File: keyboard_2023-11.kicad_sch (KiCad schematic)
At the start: 70 parts, among them J1 Conn_01x04, J11 Conn_01x07_Socket, J2 Conn_01x04_Socket, J3 Conn_01x07_Socket, J4 Conn_01x07_Pin, SW1 SW_Push, SW10 SW_Push, SW11 SW_Push, SW12 SW_Push, SW13 SW_Push, SW14 SW_Push, SW15 SW_Push, SW16 SW_Push, SW17 SW_Push, SW18 SW_Push, SW19 SW_Push, SW2 SW_Push, SW20 SW_Push, SW21 SW_Push, SW22 SW_Push, SW23 SW_Push, SW24 SW_Push, SW3 SW_Push, SW4 SW_Push, SW5 SW_Push, SW6 SW_Push, SW7 SW_Push, SW8 SW_Push, SW9 SW_Push, U1 MCP23017_SO, U2 MCP23017_SO

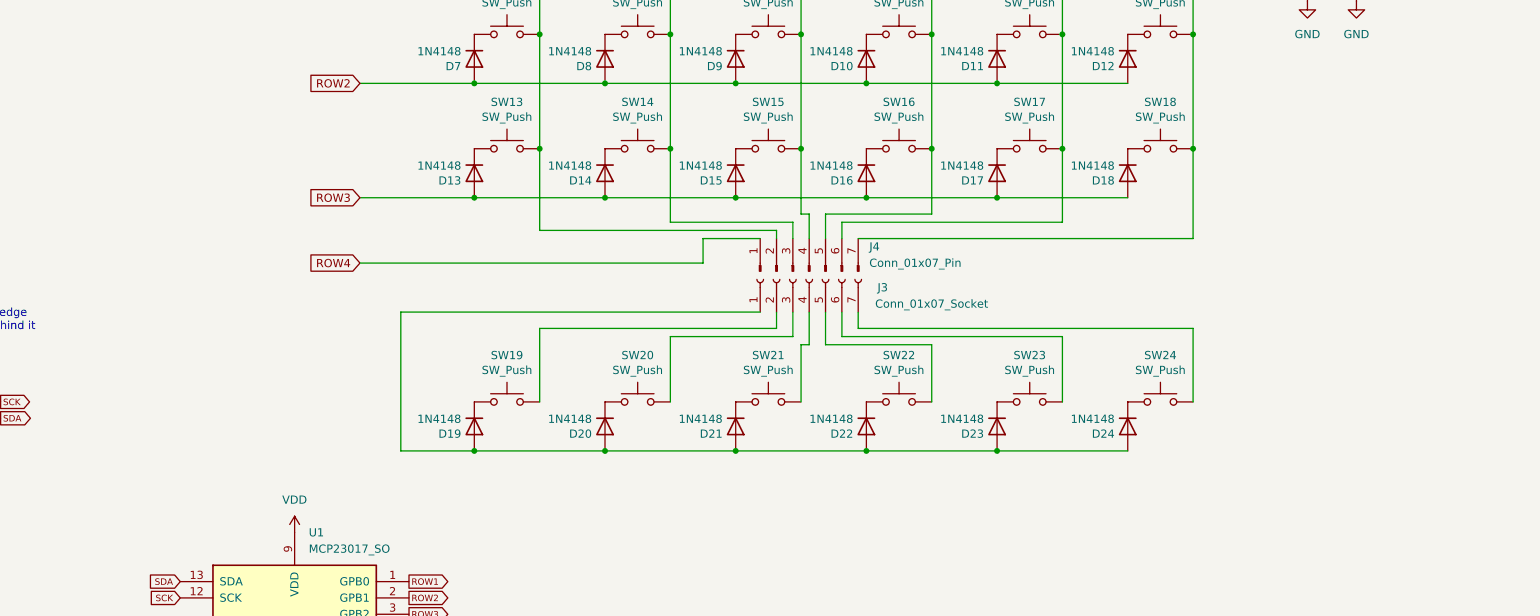
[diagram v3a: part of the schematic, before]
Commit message: better solder jumpers?
adding a solder mask cutout where the pads are default-connected, to better see which part needs to be scrached out

Signed-off-by: Johannes <you@example.com>
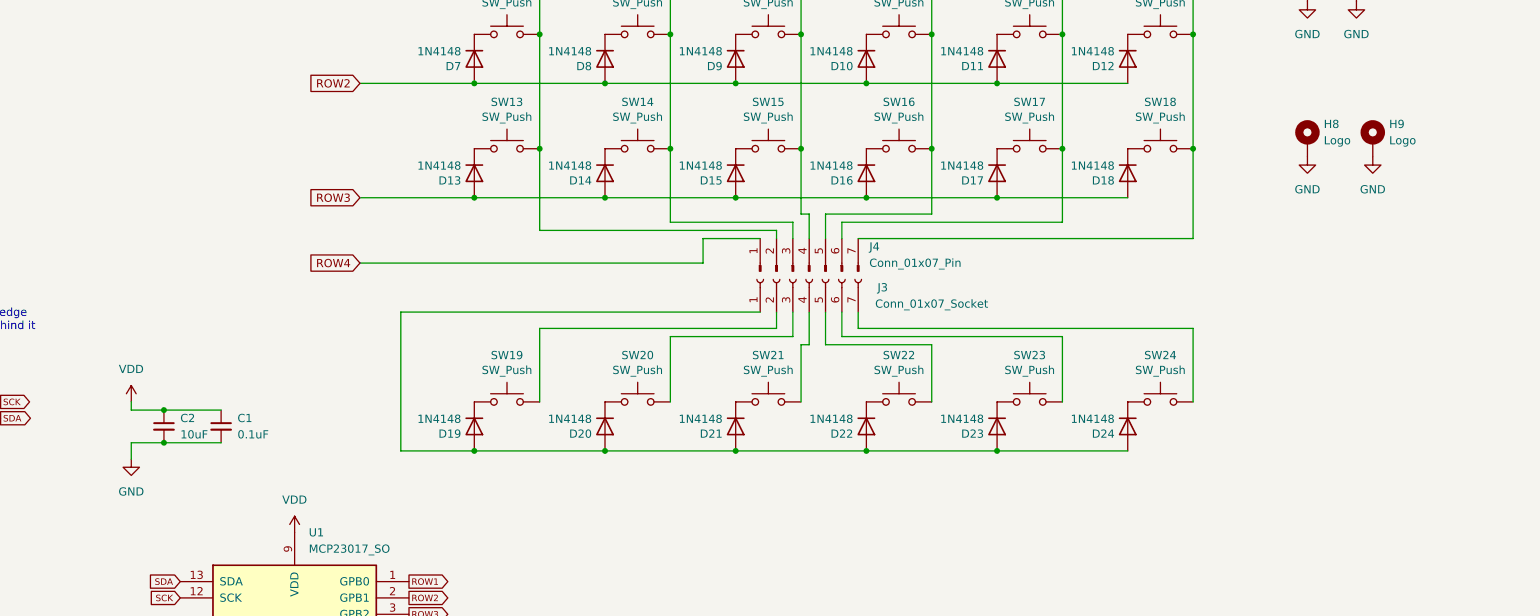
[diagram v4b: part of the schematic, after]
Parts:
- added C1: 0.1uF, reversible-kicad:C-0805_2012Metric, symbol Device:C_Small
- added C2: 10uF, reversible-kicad:C-0805_2012Metric, symbol Device:C_Small
- added H8, H9: Logo, project-local:logo, symbol Mechanical:MountingHole_Pad
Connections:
- net GND: now also C1.2, C2.2, H8.1, H9.1
- net VDD: now also C1.1, C2.1
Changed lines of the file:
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@@
 (kicad_sch (version 20230121) (generator eeschema)
   (paper "A4")
+  (junction (at 71.12 106.68) (diameter 0) (color 0 0 0 0)
+  )
   (junction (at 210.82 66.04) (diameter 0) (color 0 0 0 0)
   )
@@
   )
   (junction (at 190.5 29.21) (diameter 0) (color 0 0 0 0)
+  )
+  (junction (at 71.12 111.76) (diameter 0) (color 0 0 0 0)
   )
   (junction (at 43.18 176.53) (diameter 0) (color 0 0 0 0)
@@
     (stroke (width 0) (type default))
   )
+  (wire (pts (xy 66.04 105.41) (xy 66.04 106.68))
+    (stroke (width 0) (type default))
+  )
   (wire (pts (xy 160.02 55.88) (xy 180.34 55.88))
     (stroke (width 0) (type default))
@@
     (stroke (width 0) (type default))
   )
+  (wire (pts (xy 66.04 111.76) (xy 66.04 114.3))
+    (stroke (width 0) (type default))
+  )
+  (wire (pts (xy 66.04 106.68) (xy 71.12 106.68))
+    (stroke (width 0) (type default))
+  )
   (wire (pts (xy 119.38 113.03) (xy 139.7 113.03))
     (stroke (width 0) (type default))
@@
     (stroke (width 0) (type default))
   )
+  (wire (pts (xy 71.12 106.68) (xy 80.01 106.68))
+    (stroke (width 0) (type default))
+  )
   (wire (pts (xy 71.12 243.84) (xy 74.93 243.84))
     (stroke (width 0) (type default))
@@
     (stroke (width 0) (type default))
   )
+  (wire (pts (xy 71.12 111.76) (xy 80.01 111.76))
+    (stroke (width 0) (type default))
+  )
   (wire (pts (xy 41.91 39.37) (xy 34.29 39.37))
     (stroke (width 0) (type default))
@@
   )
   (wire (pts (xy 163.83 91.44) (xy 107.95 91.44))
+    (stroke (width 0) (type default))
+  )
+  (wire (pts (xy 71.12 111.76) (xy 66.04 111.76))
     (stroke (width 0) (type default))
   )
@@
     )
   )
+  (symbol (lib_id "power:VDD") (at 66.04 105.41 0) (unit 1)
+    (in_bom yes) (on_board yes) (dnp no) (fields_autoplaced)
+    (property "Reference" "#PWR025" (at 66.04 109.22 0)
+      (effects (font (size 1.27 1.27)) hide)
+    )
+    (property "Value" "VDD" (at 66.04 100.33 0)
+      (effects (font (size 1.27 1.27)))
+    )
+    (property "Footprint" "" (at 66.04 105.41 0)
+      (effects (font (size 1.27 1.27)) hide)
+    )
+    (property "Datasheet" "" (at 66.04 105.41 0)
+      (effects (font (size 1.27 1.27)) hide)
+    )
+    (pin "1")
+    (instances
+      (project "keyboard_2023-11"
+        (path "/182f2ae4-37a2-476f-8f08-1d2b242ef345"
+          (reference "#PWR025") (unit 1)
+        )
+      )
+    )
+  )
+  (symbol (lib_id "power:GND") (at 66.04 114.3 0) (unit 1)
+    (in_bom yes) (on_board yes) (dnp no) (fields_autoplaced)
+    (property "Reference" "#PWR026" (at 66.04 120.65 0)
+      (effects (font (size 1.27 1.27)) hide)
+    )
+    (property "Value" "GND" (at 66.04 119.38 0)
+      (effects (font (size 1.27 1.27)))
+    )
+    (property "Footprint" "" (at 66.04 114.3 0)
+      (effects (font (size 1.27 1.27)) hide)
+    )
+    (property "Datasheet" "" (at 66.04 114.3 0)
+      (effects (font (size 1.27 1.27)) hide)
+    )
+    (pin "1")
+    (instances
+      (project "keyboard_2023-11"
+        (path "/182f2ae4-37a2-476f-8f08-1d2b242ef345"
+          (reference "#PWR026") (unit 1)
+        )
+      )
+    )
+  )
   (symbol (lib_id "Device:D") (at 220.98 52.07 270) (unit 1)
     (in_bom yes) (on_board yes) (dnp no)
@@
     )
   )
+  (symbol (lib_id "Device:C_Small") (at 71.12 109.22 0) (unit 1)
+    (in_bom yes) (on_board yes) (dnp no) (fields_autoplaced)
+    (property "Reference" "C2" (at 73.66 107.9563 0)
+      (effects (font (size 1.27 1.27)) (justify left))
+    )
+    (property "Value" "10uF" (at 73.66 110.4963 0)
+      (effects (font (size 1.27 1.27)) (justify left))
+    )
+    (property "Footprint" "reversible-kicad:C-0805_2012Metric" (at 71.12 109.22 0)
+      (effects (font (size 1.27 1.27)) hide)
+    )
+    (property "Datasheet" "~" (at 71.12 109.22 0)
+      (effects (font (size 1.27 1.27)) hide)
+    )
+    (pin "1")
+    (pin "2")
+    (instances
+      (project "keyboard_2023-11"
+        (path "/182f2ae4-37a2-476f-8f08-1d2b242ef345"
+          (reference "C2") (unit 1)
+        )
+      )
+    )
+  )
+  (symbol (lib_id "Device:C_Small") (at 80.01 109.22 0) (unit 1)
+    (in_bom yes) (on_board yes) (dnp no) (fields_autoplaced)
+    (property "Reference" "C1" (at 82.55 107.9563 0)
+      (effects (font (size 1.27 1.27)) (justify left))
+    )
+    (property "Value" "0.1uF" (at 82.55 110.4963 0)
+      (effects (font (size 1.27 1.27)) (justify left))
+    )
+    (property "Footprint" "reversible-kicad:C-0805_2012Metric" (at 80.01 109.22 0)
+      (effects (font (size 1.27 1.27)) hide)
+    )
+    (property "Datasheet" "~" (at 80.01 109.22 0)
+      (effects (font (size 1.27 1.27)) hide)
+    )
+    (pin "1")
+    (pin "2")
+    (instances
+      (project "keyboard_2023-11"
+        (path "/182f2ae4-37a2-476f-8f08-1d2b242ef345"
+          (reference "C1") (unit 1)
+        )
+      )
+    )
+  )
   (symbol (lib_id "Device:D") (at 119.38 52.07 270) (unit 1)
     (in_bom yes) (on_board yes) (dnp no)
@@
     )
   )
+  (symbol (lib_id "Mechanical:MountingHole_Pad") (at 259.08 64.77 0) (unit 1)
+    (in_bom yes) (on_board yes) (dnp no) (fields_autoplaced)
+    (property "Reference" "H9" (at 261.62 62.23 0)
+      (effects (font (size 1.27 1.27)) (justify left))
+    )
+    (property "Value" "Logo" (at 261.62 64.77 0)
+      (effects (font (size 1.27 1.27)) (justify left))
+    )
+    (property "Footprint" "project-local:logo" (at 259.08 64.77 0)
+      (effects (font (size 1.27 1.27)) hide)
+    )
+    (property "Datasheet" "~" (at 259.08 64.77 0)
+      (effects (font (size 1.27 1.27)) hide)
+    )
+    (pin "1")
+    (instances
+      (project "keyboard_2023-11"
+        (path "/182f2ae4-37a2-476f-8f08-1d2b242ef345"
+          (reference "H9") (unit 1)
+        )
+      )
+    )
+  )
   (symbol (lib_id "Device:D") (at 119.38 69.85 270) (unit 1)
     (in_bom yes) (on_board yes) (dnp no)
@@
         (path "/c9658e9c-05d2-4fe9-b3ad-fb43f9141d6f"
           (reference "D17") (unit 1)
+        )
+      )
+    )
+  )
+  (symbol (lib_id "power:GND") (at 248.92 67.31 0) (unit 1)
+    (in_bom yes) (on_board yes) (dnp no) (fields_autoplaced)
+    (property "Reference" "#PWR027" (at 248.92 73.66 0)
+      (effects (font (size 1.27 1.27)) hide)
+    )
+    (property "Value" "GND" (at 248.92 72.39 0)
+      (effects (font (size 1.27 1.27)))
+    )
+    (property "Footprint" "" (at 248.92 67.31 0)
+      (effects (font (size 1.27 1.27)) hide)
+    )
+    (property "Datasheet" "" (at 248.92 67.31 0)
+      (effects (font (size 1.27 1.27)) hide)
+    )
+    (pin "1")
+    (instances
+      (project "keyboard_2023-11"
+        (path "/182f2ae4-37a2-476f-8f08-1d2b242ef345"
+          (reference "#PWR027") (unit 1)
         )
       )
@@
     )
   )
+  (symbol (lib_id "Mechanical:MountingHole_Pad") (at 248.92 64.77 0) (unit 1)
+    (in_bom yes) (on_board yes) (dnp no) (fields_autoplaced)
+    (property "Reference" "H8" (at 251.46 62.23 0)
+      (effects (font (size 1.27 1.27)) (justify left))
+    )
+    (property "Value" "Logo" (at 251.46 64.77 0)
+      (effects (font (size 1.27 1.27)) (justify left))
+    )
+    (property "Footprint" "project-local:logo" (at 248.92 64.77 0)
+      (effects (font (size 1.27 1.27)) hide)
+    )
+    (property "Datasheet" "~" (at 248.92 64.77 0)
+      (effects (font (size 1.27 1.27)) hide)
+    )
+    (pin "1")
+    (instances
+      (project "keyboard_2023-11"
+        (path "/182f2ae4-37a2-476f-8f08-1d2b242ef345"
+          (reference "H8") (unit 1)
+        )
+      )
+    )
+  )
   (symbol (lib_id "Switch:SW_Push") (at 226.06 48.26 0) (unit 1)
     (in_bom yes) (on_board yes) (dnp no)
@@
         )
       )
+    )
+  )
+  (symbol (lib_id "power:GND") (at 259.08 67.31 0) (unit 1)
+    (in_bom yes) (on_board yes) (dnp no) (fields_autoplaced)
+    (property "Reference" "#PWR028" (at 259.08 73.66 0)
+      (effects (font (size 1.27 1.27)) hide)
+    )
+    (property "Value" "GND" (at 259.08 72.39 0)
+      (effects (font (size 1.27 1.27)))
+    )
+    (property "Footprint" "" (at 259.08 67.31 0)
+      (effects (font (size 1.27 1.27)) hide)
+    )
+    (property "Datasheet" "" (at 259.08 67.31 0)
+      (effects (font (size 1.27 1.27)) hide)
+    )
+    (pin "1")
+    (instances
+      (project "keyboard_2023-11"
+        (path "/182f2ae4-37a2-476f-8f08-1d2b242ef345"
+          (reference "#PWR028") (unit 1)
+        )
+      )
